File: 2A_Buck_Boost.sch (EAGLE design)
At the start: 29 parts, among them U1 TPS63070

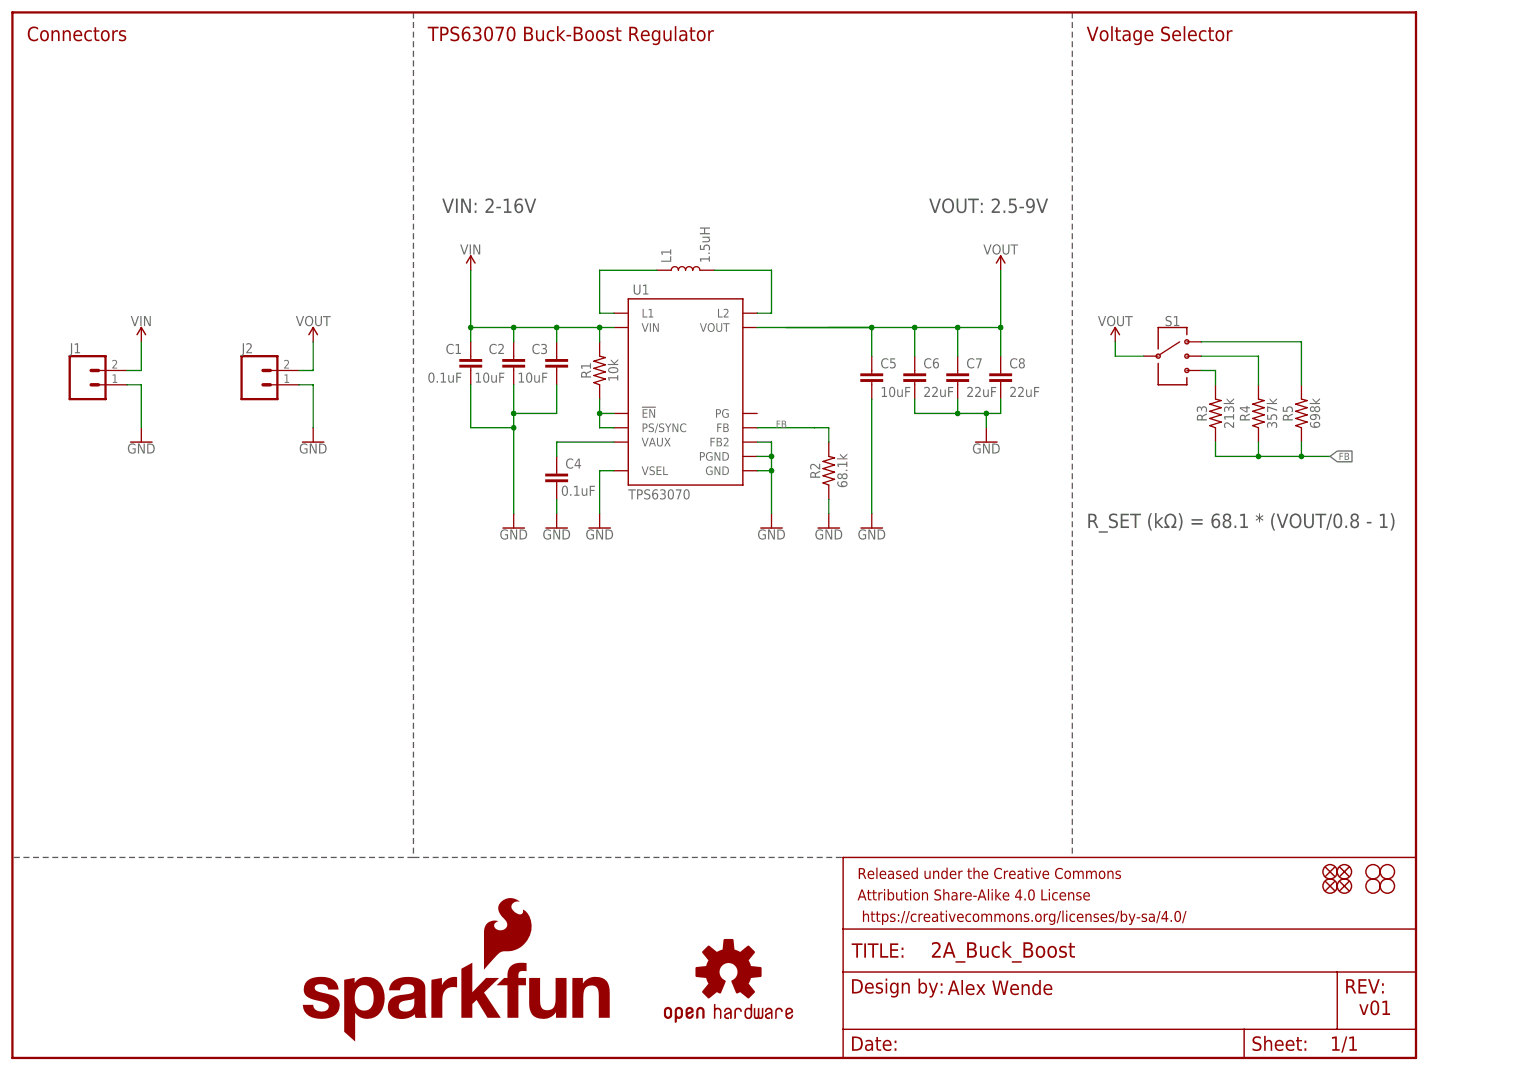
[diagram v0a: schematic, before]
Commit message: Design Review Changes
-Moved standoffs 0.1" offset
-Added power LED with jumper to output
-Added vias under IC1
-Added units to measures layer
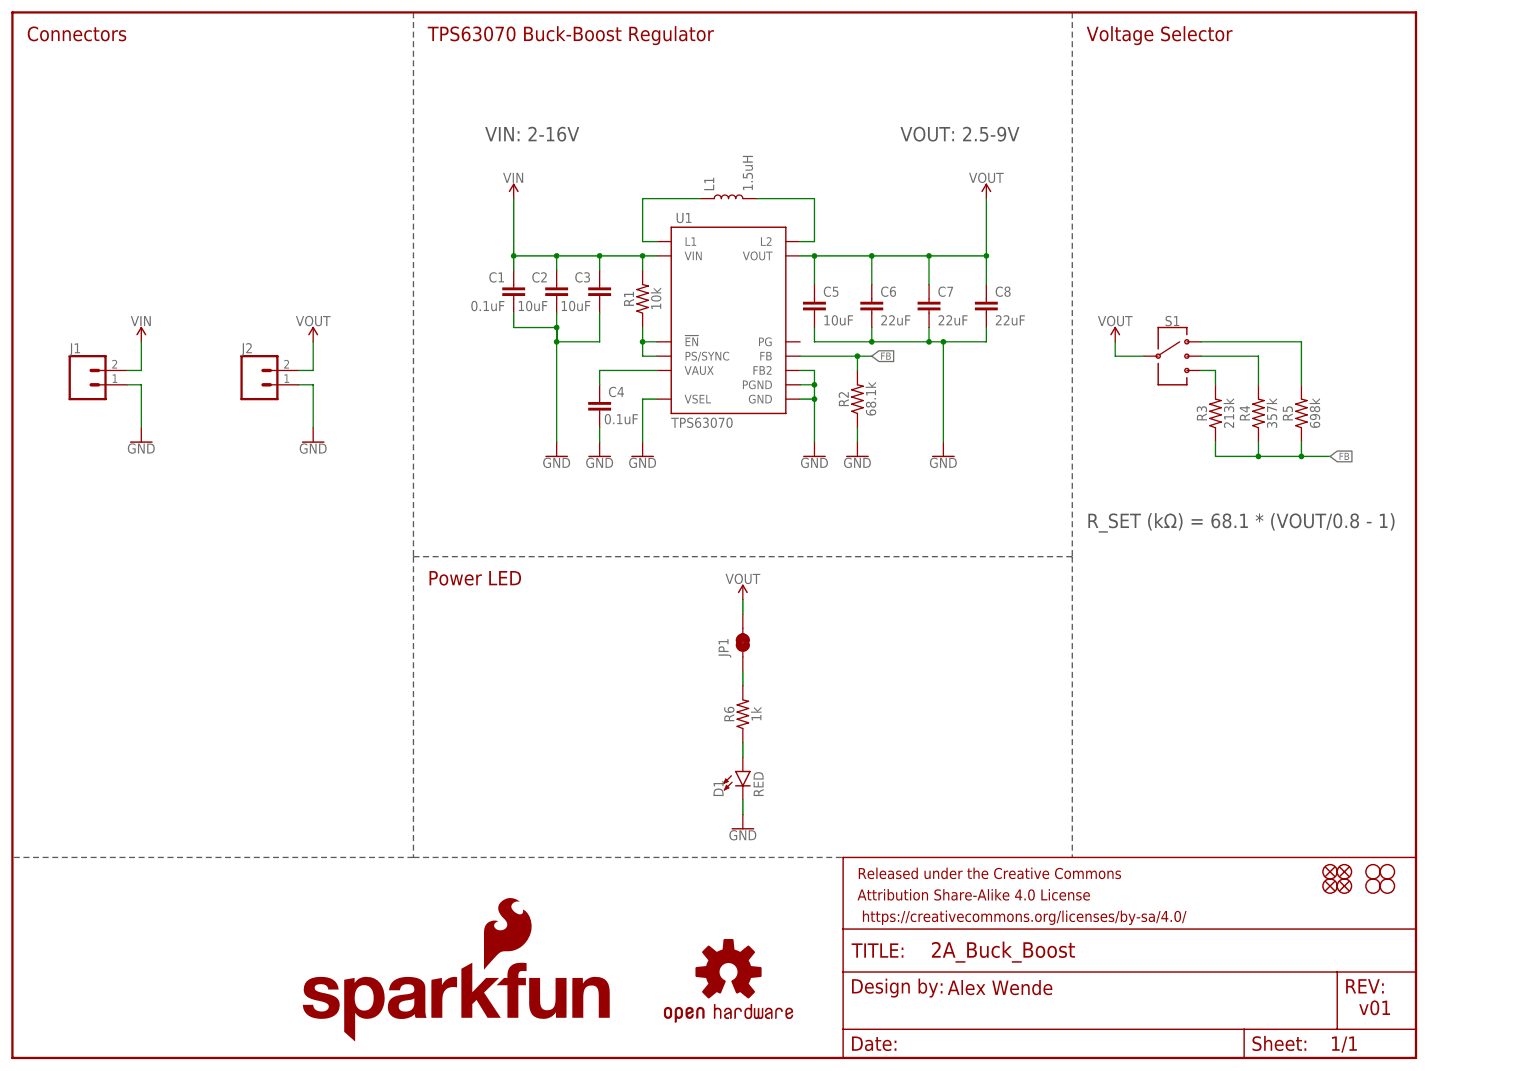
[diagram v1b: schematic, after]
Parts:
- added D1: RED, SparkFun-LED:LED-RED0603
- added JP1: JUMPER-SMT_2_NC_TRACE_NO-SILK, SparkFun-Jumpers:JUMPER-SMT_2_NC_TRACE_NO-SILK
- added R6: 1k, SparkFun-Resistors:1KOHM-0603-1/10W-1%
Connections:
- new net N$8: JP1.1, R6.2
- new net N$9: D1.A, R6.1
- net GND: now also D1.C
- net VOUT: now also JP1.2
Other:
- note added: "Power LED"
- moved on the sheet: C1, C2, C3, C4, C5, C6, C7, C8, L1, R1, R2, U1

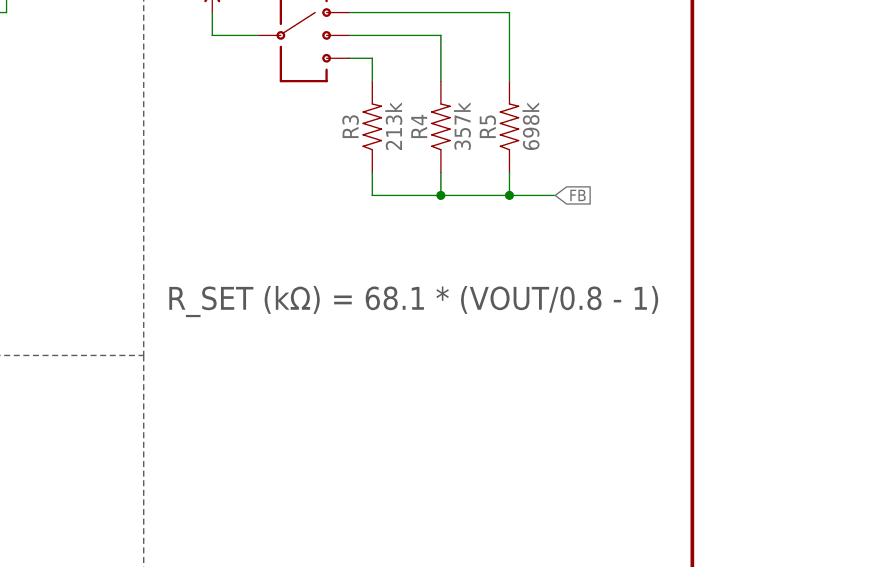
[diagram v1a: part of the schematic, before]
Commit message: QC Fixes
-Fixed board dimention width
-Fixed feedback resistor equation
-Adjusted power led silk
-Adjusted VIN copper pour to line up with C1 tstop
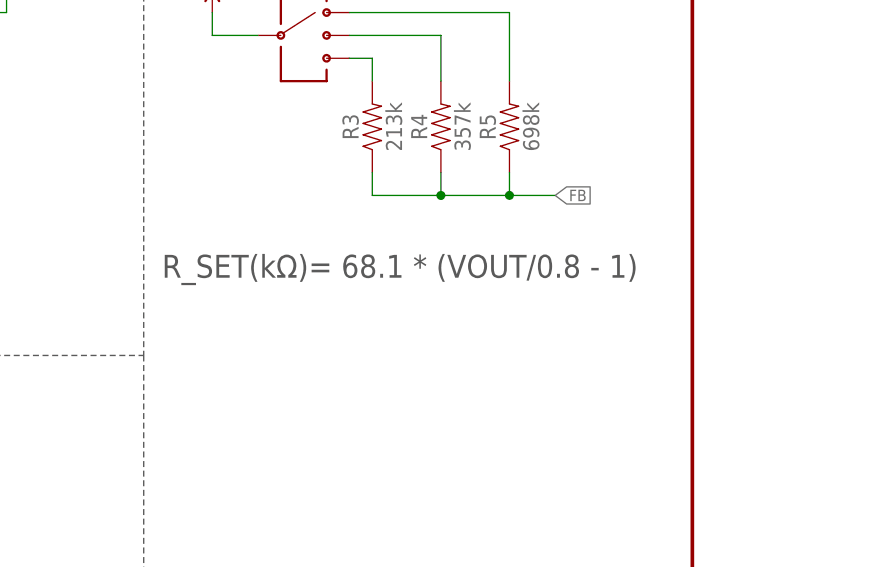
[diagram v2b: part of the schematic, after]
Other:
- note added: "R_SET(kΩ)= 68.1 * (VOUT/0.8 - 1)"
- note removed: "R_SET (kΩ) = 68.1 * (VOUT/0.8 - 1)"
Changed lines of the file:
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@@
 <text x="83.82" y="162.56" size="2.54" layer="97" font="vector">VIN: 2-16V</text>
 <text x="157.48" y="162.56" size="2.54" layer="97" font="vector">VOUT: 2.5-9V</text>
-<text x="190.5" y="93.98" size="2.54" layer="97" font="vector">R_SET (kΩ) = 68.1 * (VOUT/0.8 - 1)</text>
+<text x="189.992" y="97.536" size="2.54" layer="97" font="vector">R_SET(kΩ)= 68.1 * (VOUT/0.8 - 1)</text>
 <wire x1="187.96" y1="88.9" x2="187.96" y2="35.56" width="0.1524" layer="97" style="shortdash"/>
 <wire x1="71.12" y1="88.9" x2="187.96" y2="88.9" width="0.1524" layer="97" style="shortdash"/>
